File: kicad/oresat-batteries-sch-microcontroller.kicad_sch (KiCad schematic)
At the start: 51 parts, among them J4 ORESAT-DEBUG-CONNECTOR-ALL, Q20 PMV45EN, Q21 PMV45EN, Q38 PMV45EN, Q39 PMV45EN, Q42 MOSFET-PCH-SOT23-6, Q43 MOSFET-PCH-SOT23-6, U20 TCAN330, U21 STM32F091C, X3 CRYSTAL-WITH-GND

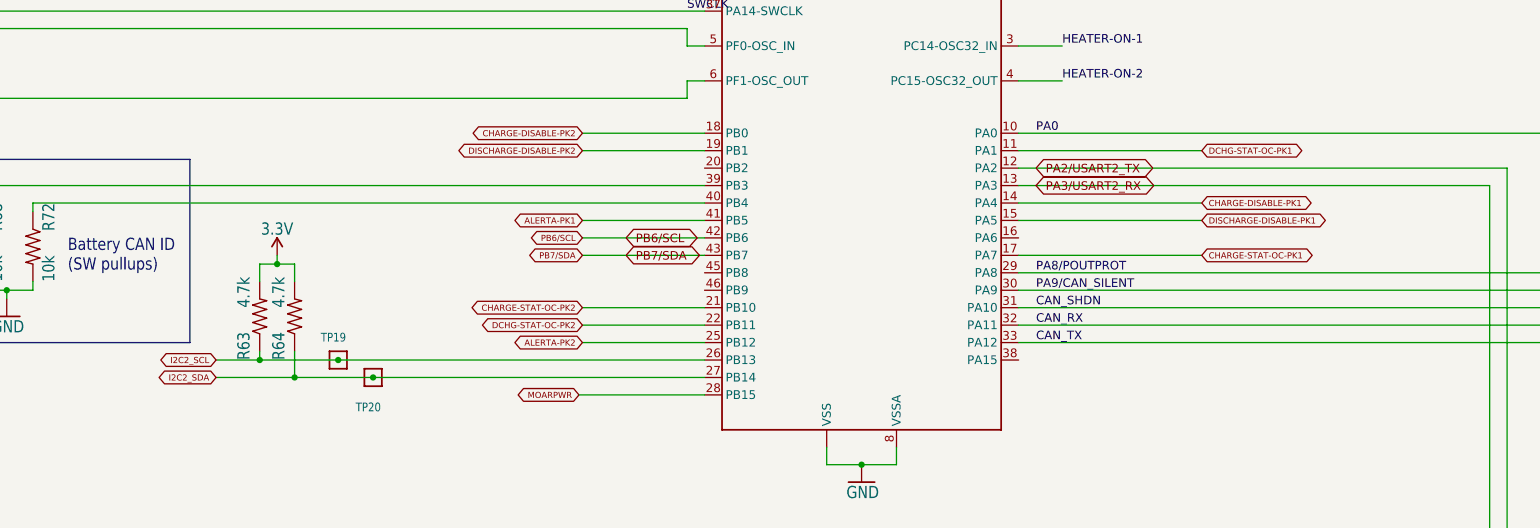
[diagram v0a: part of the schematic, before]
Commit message: Move main connector to kicad libraries; start updating text size.
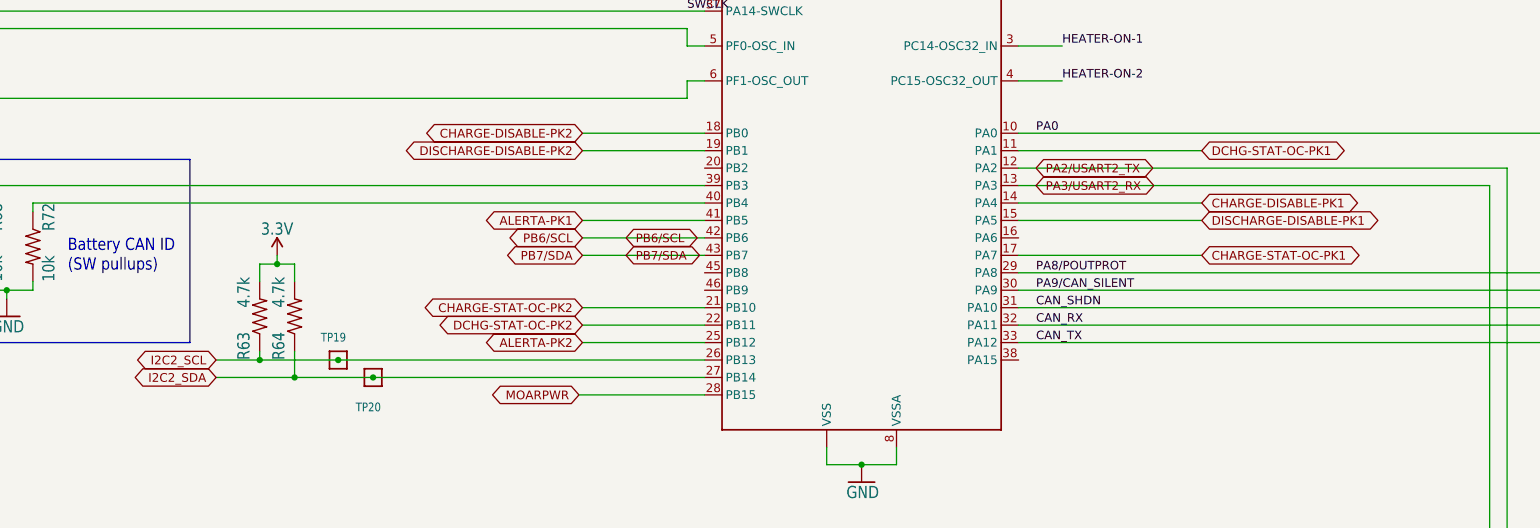
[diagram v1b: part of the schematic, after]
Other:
- title: OreSat Battery Card -> OreSat Battery Card - Microcontroller
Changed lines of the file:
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@@
   (paper "B")
   (title_block
-    (title "OreSat Battery Card")
+    (title "OreSat Battery Card - Microcontroller")
     (date "2023-12-02")
     (rev "3.1")
@@
   )
   (global_label "PB7/SDA" (shape bidirectional) (at 190.5 99.06 180) (fields_autoplaced)
-    (effects (font (size 0.889 0.889)) (justify right))
+    (effects (font (size 1.27 1.27)) (justify right))
     (property "Intersheetrefs" "${INTERSHEET_REFS}" (at 181.5789 99.06 0)
       (effects (font (size 1.27 1.27)) (justify right) hide)
@@
   )
   (global_label "DISCHARGE-DISABLE-PK2" (shape bidirectional) (at 190.5 83.82 180) (fields_autoplaced)
-    (effects (font (size 0.889 0.889)) (justify right))
+    (effects (font (size 1.27 1.27)) (justify right))
     (property "Intersheetrefs" "${INTERSHEET_REFS}" (at 170.1489 83.82 0)
       (effects (font (size 1.27 1.27)) (justify right) hide)
@@
   )
   (global_label "CHARGE-STAT-OC-PK2" (shape bidirectional) (at 190.5 106.68 180) (fields_autoplaced)
-    (effects (font (size 0.889 0.889)) (justify right))
+    (effects (font (size 1.27 1.27)) (justify right))
     (property "Intersheetrefs" "${INTERSHEET_REFS}" (at 171.7576 106.68 0)
       (effects (font (size 1.27 1.27)) (justify right) hide)
@@
   )
   (global_label "DISCHARGE-DISABLE-PK1" (shape bidirectional) (at 280.67 93.98 0) (fields_autoplaced)
-    (effects (font (size 0.889 0.889)) (justify left))
+    (effects (font (size 1.27 1.27)) (justify left))
     (property "Intersheetrefs" "${INTERSHEET_REFS}" (at 301.0211 93.98 0)
       (effects (font (size 1.27 1.27)) (justify left) hide)
@@
   )
   (global_label "DCHG-STAT-OC-PK1" (shape bidirectional) (at 280.67 83.82 0) (fields_autoplaced)
-    (effects (font (size 0.889 0.889)) (justify left))
+    (effects (font (size 1.27 1.27)) (justify left))
     (property "Intersheetrefs" "${INTERSHEET_REFS}" (at 297.8461 83.82 0)
       (effects (font (size 1.27 1.27)) (justify left) hide)
@@
   )
   (global_label "CHARGE-DISABLE-PK1" (shape bidirectional) (at 280.67 91.44 0) (fields_autoplaced)
-    (effects (font (size 0.889 0.889)) (justify left))
+    (effects (font (size 1.27 1.27)) (justify left))
     (property "Intersheetrefs" "${INTERSHEET_REFS}" (at 298.8621 91.44 0)
       (effects (font (size 1.27 1.27)) (justify left) hide)
@@
   )
   (global_label "CHARGE-DISABLE-PK2" (shape bidirectional) (at 190.5 81.28 180) (fields_autoplaced)
-    (effects (font (size 0.889 0.889)) (justify right))
+    (effects (font (size 1.27 1.27)) (justify right))
     (property "Intersheetrefs" "${INTERSHEET_REFS}" (at 172.3079 81.28 0)
       (effects (font (size 1.27 1.27)) (justify right) hide)
@@
   )
   (global_label "ALERTA-PK2" (shape bidirectional) (at 190.5 111.76 180) (fields_autoplaced)
-    (effects (font (size 0.889 0.889)) (justify right))
+    (effects (font (size 1.27 1.27)) (justify right))
     (property "Intersheetrefs" "${INTERSHEET_REFS}" (at 179.2929 111.76 0)
       (effects (font (size 1.27 1.27)) (justify right) hide)
@@
   )
   (global_label "CHARGE-STAT-OC-PK1" (shape bidirectional) (at 280.67 99.06 0) (fields_autoplaced)
-    (effects (font (size 0.889 0.889)) (justify left))
+    (effects (font (size 1.27 1.27)) (justify left))
     (property "Intersheetrefs" "${INTERSHEET_REFS}" (at 299.4124 99.06 0)
       (effects (font (size 1.27 1.27)) (justify left) hide)
@@
   )
   (global_label "ALERTA-PK1" (shape bidirectional) (at 190.5 93.98 180) (fields_autoplaced)
-    (effects (font (size 0.889 0.889)) (justify right))
+    (effects (font (size 1.27 1.27)) (justify right))
     (property "Intersheetrefs" "${INTERSHEET_REFS}" (at 179.2929 93.98 0)
       (effects (font (size 1.27 1.27)) (justify right) hide)
@@
   )
   (global_label "DCHG-STAT-OC-PK2" (shape bidirectional) (at 190.5 109.22 180) (fields_autoplaced)
-    (effects (font (size 0.889 0.889)) (justify right))
+    (effects (font (size 1.27 1.27)) (justify right))
     (property "Intersheetrefs" "${INTERSHEET_REFS}" (at 173.3239 109.22 0)
       (effects (font (size 1.27 1.27)) (justify right) hide)
@@
   )
   (global_label "MOARPWR" (shape bidirectional) (at 189.992 119.38 180) (fields_autoplaced)
-    (effects (font (size 0.889 0.889)) (justify right))
+    (effects (font (size 1.27 1.27)) (justify right))
     (property "Intersheetrefs" "${INTERSHEET_REFS}" (at 180.7323 119.38 0)
       (effects (font (size 1.27 1.27)) (justify right) hide)
@@
   )
   (global_label "PB6/SCL" (shape bidirectional) (at 190.5 96.52 180) (fields_autoplaced)
-    (effects (font (size 0.889 0.889)) (justify right))
+    (effects (font (size 1.27 1.27)) (justify right))
     (property "Intersheetrefs" "${INTERSHEET_REFS}" (at 181.6212 96.52 0)
       (effects (font (size 1.27 1.27)) (justify right) hide)
@@
   )
   (global_label "I2C2_SDA" (shape bidirectional) (at 137.16 116.84 180) (fields_autoplaced)
-    (effects (font (size 0.889 0.889)) (justify right))
+    (effects (font (size 1.27 1.27)) (justify right))
     (property "Intersheetrefs" "${INTERSHEET_REFS}" (at 128.1119 116.84 0)
       (effects (font (size 1.27 1.27)) (justify right) hide)
@@
   )
   (global_label "I2C2_SCL" (shape bidirectional) (at 137.16 114.3 180) (fields_autoplaced)
-    (effects (font (size 0.889 0.889)) (justify right))
+    (effects (font (size 1.27 1.27)) (justify right))
     (property "Intersheetrefs" "${INTERSHEET_REFS}" (at 128.1542 114.3 0)
       (effects (font (size 1.27 1.27)) (justify right) hide)

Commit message: Updated ground planes, battery foot prints, zones needs more work.
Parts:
- D11, D12, D4, D9: footprint oresat-batteries:SOD323-R -> Diode_SMD:D_SOD-323; symbol oresat-batteries-eagle-import:DIODE-SOD323-R -> oresat-diodes:1N4151WS-HE3; DIS Digi-Key -> (none); DPN 112-1N4151WS-E3-08CT-ND -> (none); MFR Vishay -> (none); MPN 1N4151WS-E3-08 -> (none)
- X3: value CRYSTAL-WITH-GND -> ECS-160-10-36Q-ES-TR
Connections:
- net PB6/SCL: no longer U21.42 (PB6)
- net PB7/SDA: no longer U21.43 (PB7)
- net at Q43.1 (G), R43.2: now also D12.2; no longer D12.A
- net at Q42.3 (G), R41.2: now also D4.2; no longer D4.A
- net at Q42.1 (G), R40.2: now also D9.2; no longer D9.A
- net at Q43.3 (G), R42.2: now also D11.2; no longer D11.A
- net PA2/USART2_TX renamed PA2/USART2_TX
- net PA3/USART2_RX renamed PA3/USART2_RX
- new net: D11.1, D12.1, D4.1, D9.1, Q38.3 (D), Q39.3 (D)
- new net PB6/SCL: U21.42 (PB6)
- new net PB7/SDA: U21.43 (PB7)
- no-connect marks 0 -> 10
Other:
- moved on the sheet: C46, C47, R63, R64, R68, R72, TP19, TP20, X3

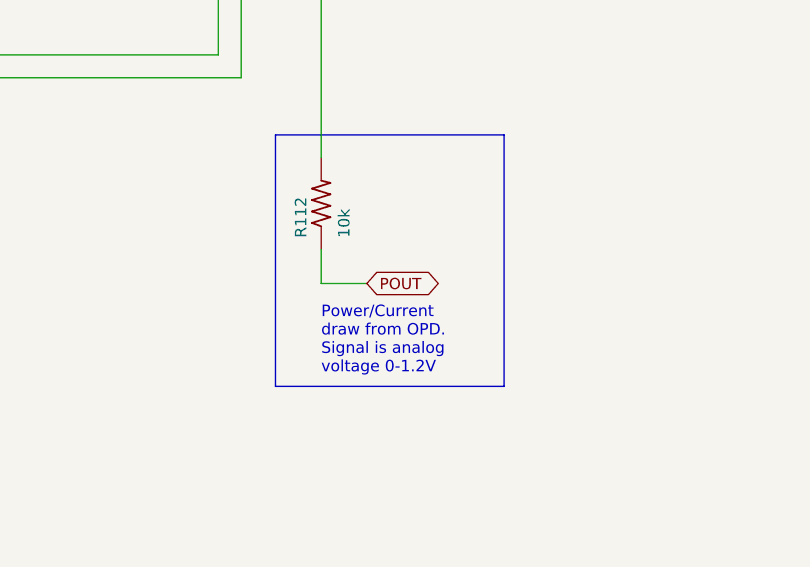
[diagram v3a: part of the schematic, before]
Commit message: better schematic layout (no netlist changes) on battery packs, and updated DRUs and fixed some minor DRU issues.
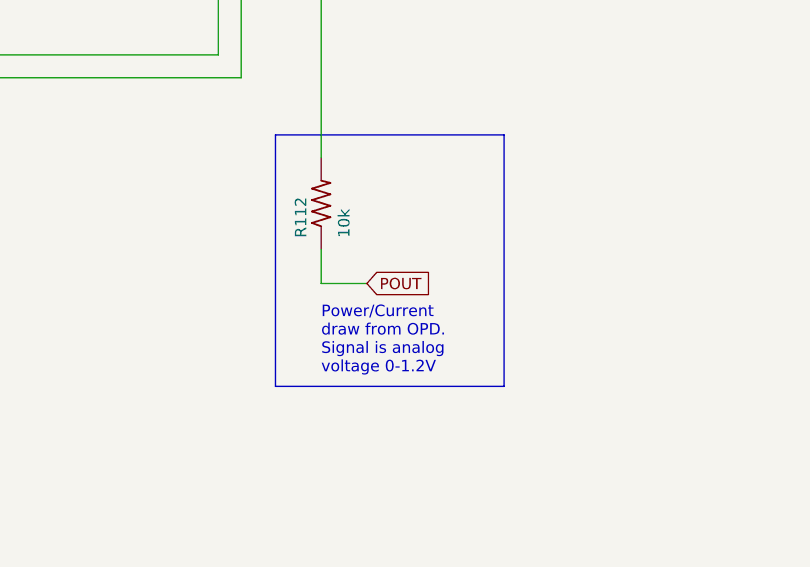
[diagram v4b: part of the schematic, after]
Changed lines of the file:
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@@
     )
   )
-  (global_label "POUT" (shape bidirectional) (at 350.52 171.45 0) (fields_autoplaced)
+  (global_label "POUT" (shape input) (at 350.52 171.45 0) (fields_autoplaced)
     (effects (font (size 1.2446 1.2446)) (justify left))
-    (property "Intersheetrefs" "${INTERSHEET_REFS}" (at 359.3349 171.45 0)
+    (property "Intersheetrefs" "${INTERSHEET_REFS}" (at 358.2459 171.45 0)
       (effects (font (size 1.27 1.27)) (justify left))
     )

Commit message: Starting Battery Card 4.0
Changed root sheet to hierarchical sheet. No change to schematic or layout yet. Updated the stackup with oresat template. Switched to variables for version and date.
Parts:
- removed D11, D12, D4, D9: 1N4151WS, Diode_SMD:D_SOD-323, symbol oresat-diodes:1N4151WS-HE3
- removed JP14, JP15, JP16, JP17: PINHD-1X1, oresat-batteries:1X01, symbol oresat-batteries-eagle-import:PINHD-1X1
- removed Q20, Q21, Q38, Q39: PMV45EN, oresat-batteries:SOT23-3, symbol oresat-batteries-eagle-import:N-MOSFET-SOT-23-3
- removed Q42, Q43: MOSFET-PCH-SOT23-6, oresat-batteries:SOT23-6, symbol oresat-batteries-eagle-import:Q-MOSFET-PCH-dual-SOT23-6_MOSFET-PCH-SOT23-6
- removed R105, R106, R40, R41, R42, R43: 10k, oresat-batteries:.0603-C-NOSILK, symbol oresat-batteries-eagle-import:R-US_0603-C-NOSILK
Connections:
- net PB6/SCL is gone; now on net PB6/SCL: R113.1, TP21.1
- net PB7/SDA is gone; now on net PB7/SDA: R114.1, TP22.1
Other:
- note added: "ALL CAPS ARE 0603, 10%, X5R or better, AEQ, Vw >= 25 V UNLESS OTHERWISE NOTED ALL RESISTORS ARE 0603 1% AEQ UNLESS OTHERWISE NOTED."
- note removed: "+Y HEATER"
- note removed: "-Y HEATER"
- note removed: "2x Minco HK6903 Heaters (12.7 x 101.6 mm @ 49 ohm)"
- note removed: "ALL CAPS ARE 0603, 10%, X5R, WV >= 16 V UNLESS OTHERWISE NOTED ALL RESISTORS ARE 0603 1% UNLESS OTHERWISE NOTED"
- note removed: "HEATER"
- note removed: "NOTE: UC must assert MOARPWR in order not to trip the OPD circuit breaker when running the heaters~{}"
- company: (none) -> Portland State Aerospace Society
- title: OreSat Battery Card - Microcontroller -> OreSat Battery Card
